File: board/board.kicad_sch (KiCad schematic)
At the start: 33 parts, among them J2 Conn_01x10, J3 Conn_01x06, J4 Conn_01x02, J5 Conn_01x06, J7 Conn_01x30, U2 nPM1300-QEAA, U3 MDBT50Q-P1MV2, Y1 32k Hz

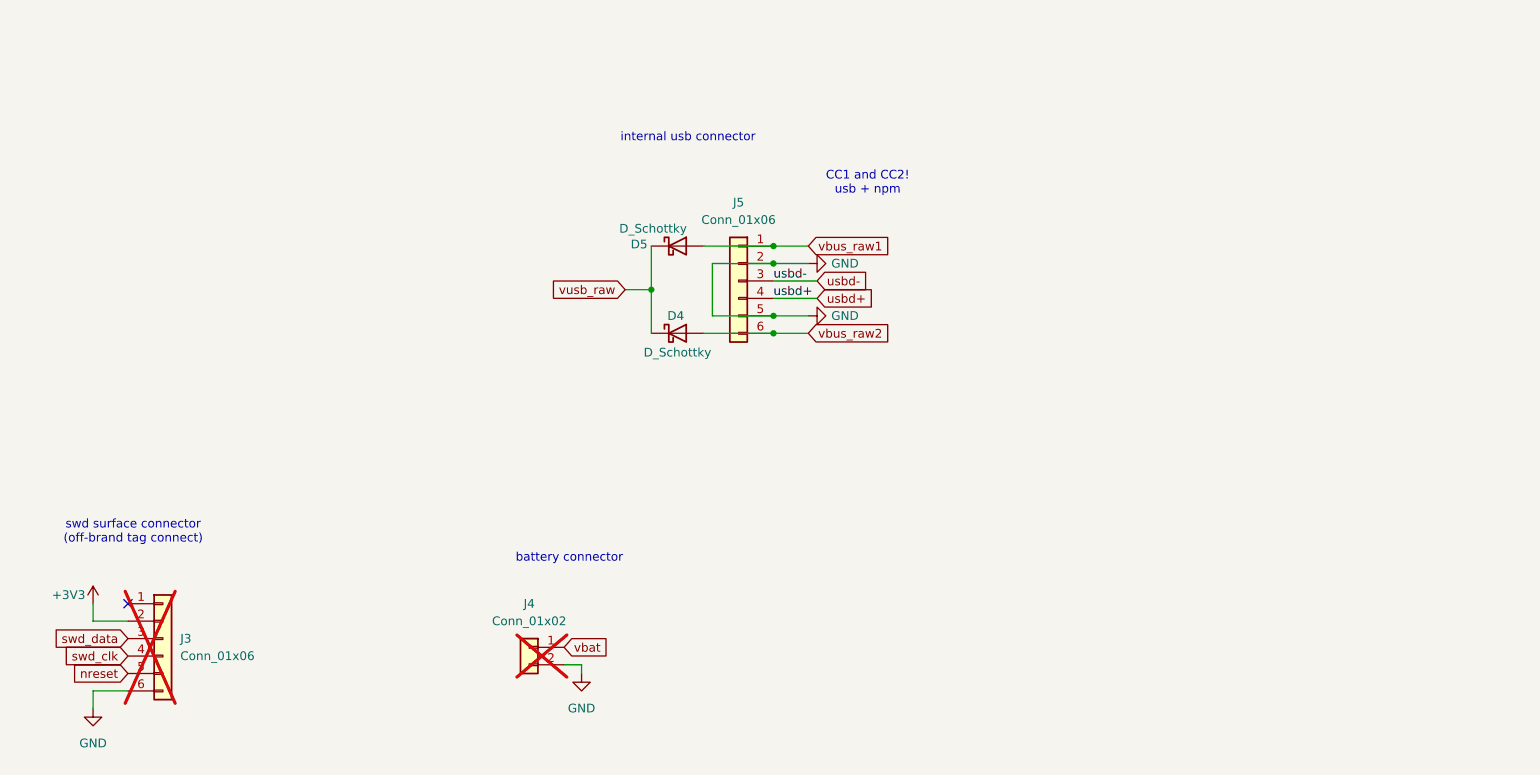
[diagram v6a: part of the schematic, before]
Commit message: board: sch add usb c to magnet adapter
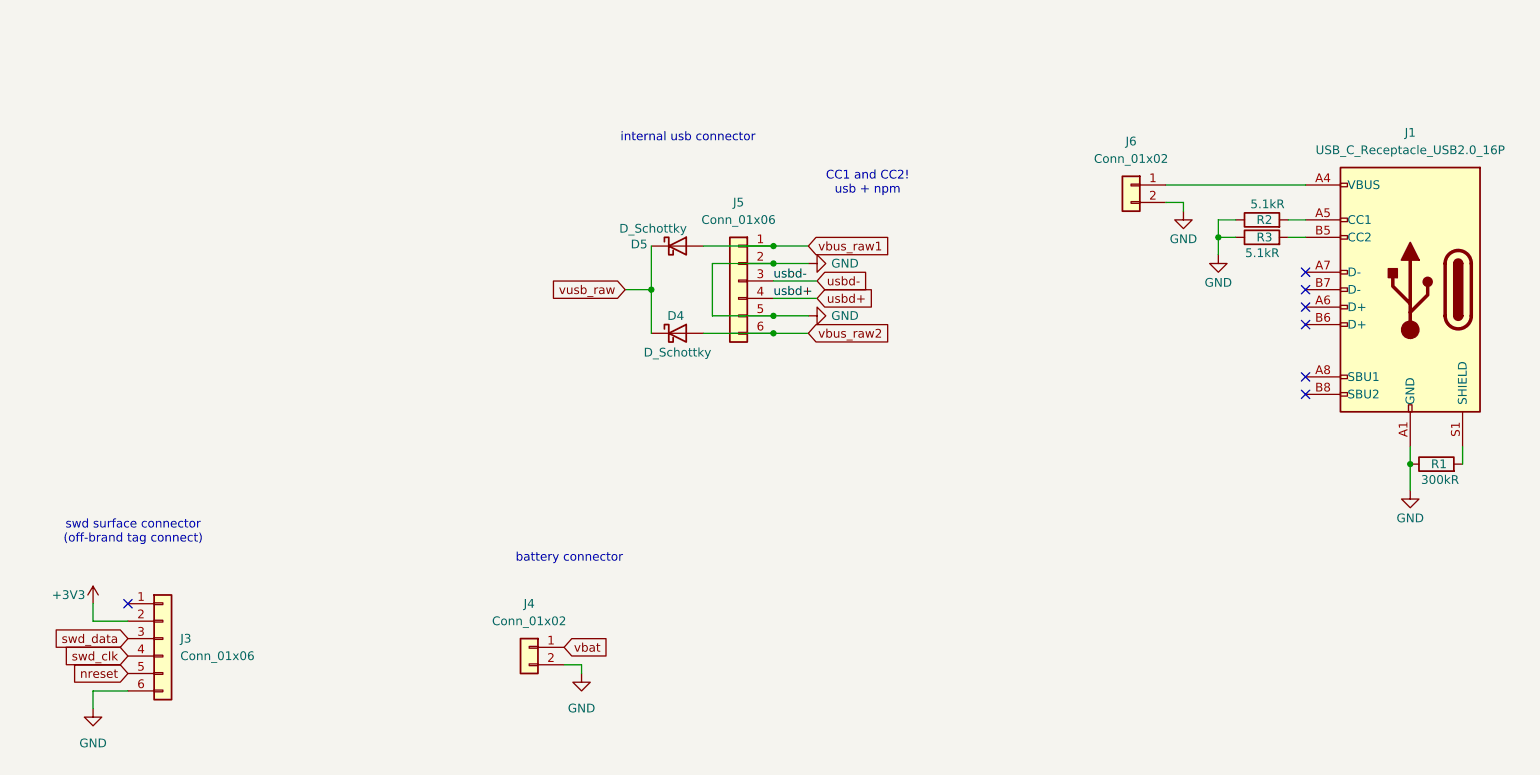
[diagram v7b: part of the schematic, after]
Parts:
- added J1: USB_C_Receptacle_USB2.0_16P, symbol Connector:USB_C_Receptacle_USB2.0_16P
- added J6: Conn_01x02, phiboard:magnetic connector 01x02P, symbol Connector_Generic:Conn_01x02
- added R1: 300kR, Resistor_SMD:R_0201_0603Metric, symbol Device:R
- added R2, R3: 5.1kR, Resistor_SMD:R_0201_0603Metric, symbol Device:R
- J3, J4: now fitted; now in the parts list
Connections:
- net GND: now also J1.A1 (GND), J1.A12 (GND), J1.B1 (GND), J1.B12 (GND), J6.2 (Pin_2), R1.1, R2.1, R3.1
- new net: J1.A4 (VBUS), J1.A9 (VBUS), J1.B4 (VBUS), J1.B9 (VBUS), J6.1 (Pin_1)
- new net: J1.S1 (SHIELD), R1.2
- new net: J1.B5 (CC2), R3.2
- new net: J1.A5 (CC1), R2.2
- no-connect marks 13 -> 19

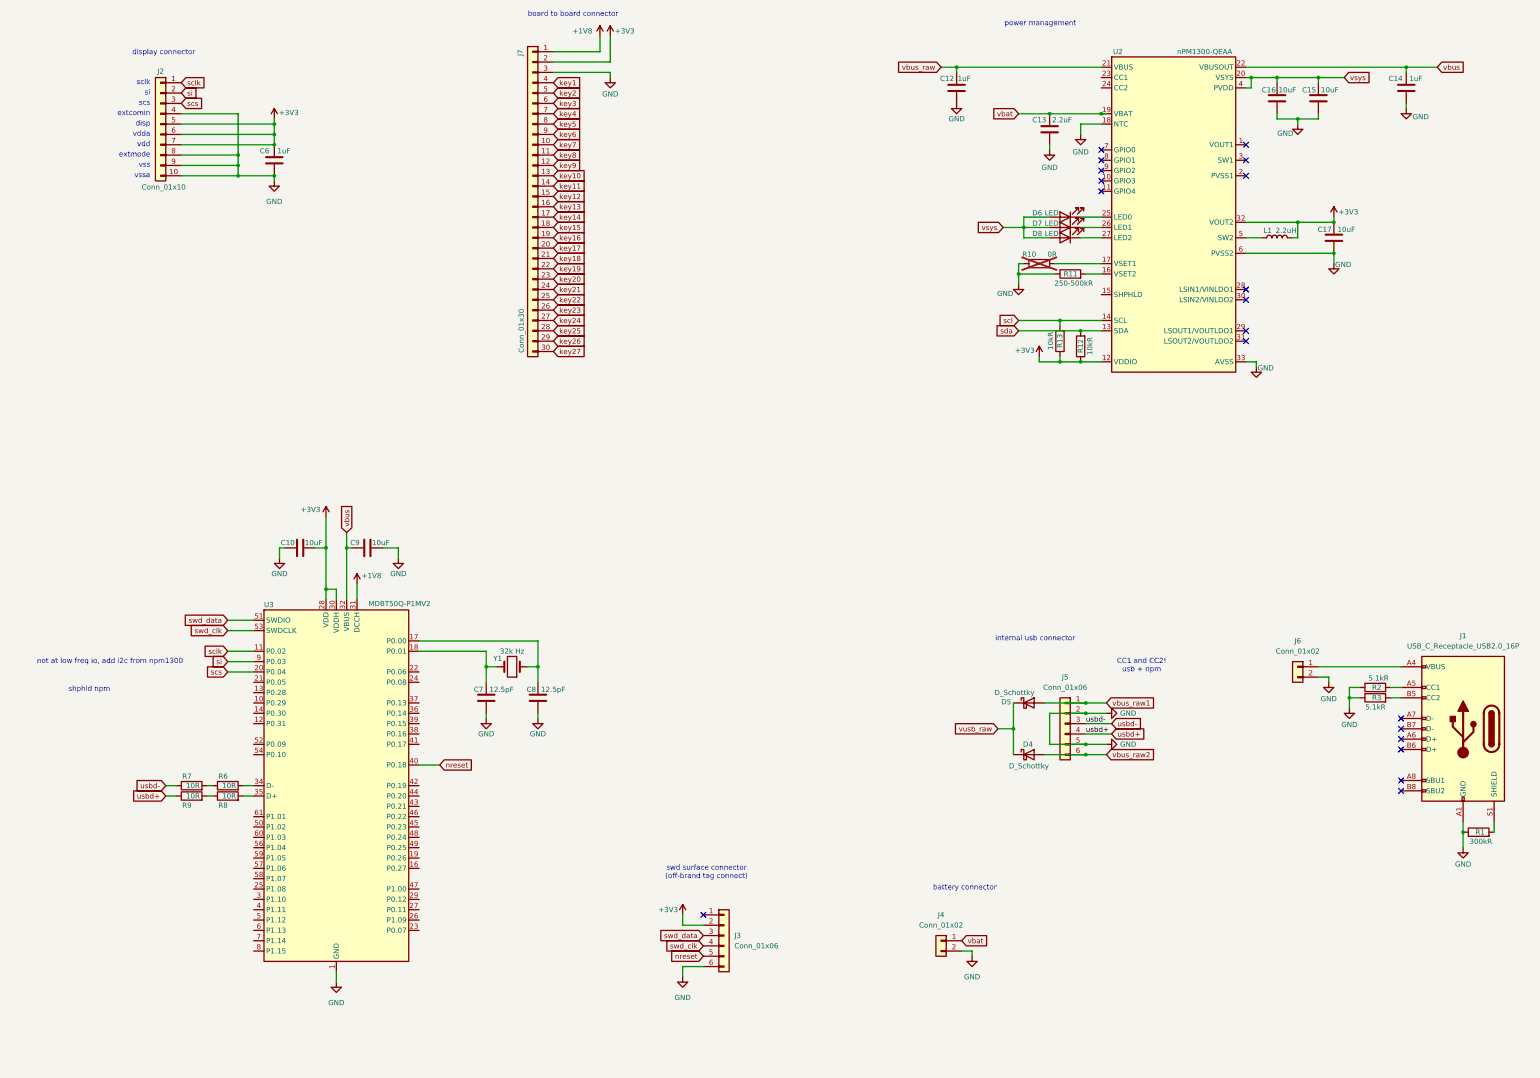
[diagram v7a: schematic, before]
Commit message: board: sch add usb circuit
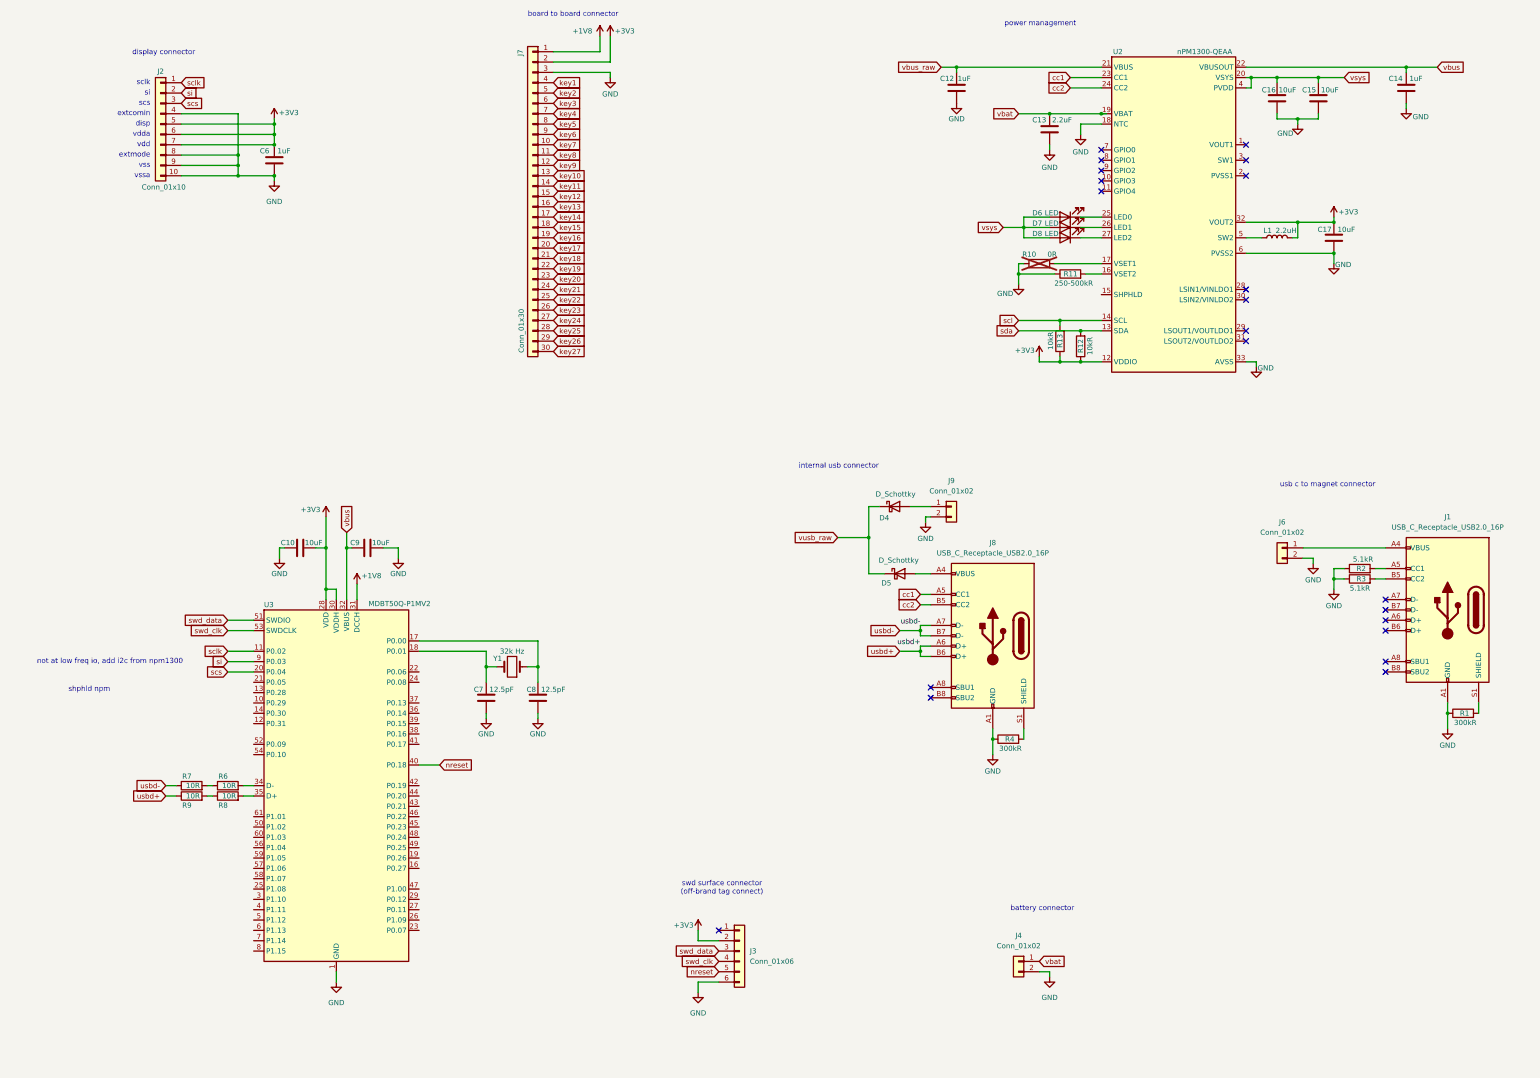
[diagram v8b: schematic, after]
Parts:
- removed J5: Conn_01x06, symbol Connector_Generic:Conn_01x06
- added J8: USB_C_Receptacle_USB2.0_16P, symbol Connector:USB_C_Receptacle_USB2.0_16P
- added J9: Conn_01x02, phiboard:magnetic connector 01x02P, symbol Connector_Generic:Conn_01x02
- added R4: 300kR, Resistor_SMD:R_0201_0603Metric, symbol Device:R
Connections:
- net GND: now also J8.A1 (GND), J8.A12 (GND), J8.B1 (GND), J8.B12 (GND), J9.2 (Pin_2), R4.1
- net usbd+: now also J8.A6 (D+), J8.B6 (D+)
- net usbd-: now also J8.A7 (D-), J8.B7 (D-)
- net cc1: now reaches U2.23 (CC1)
- net cc1: now also J8.A5 (CC1)
- net cc2: now reaches U2.24 (CC2)
- net cc2: now also J8.B5 (CC2)
- net vbus_raw1: no longer names the net of D5.2 (A)
- net vbus_raw1: now also J8.A4 (VBUS), J8.A9 (VBUS), J8.B4 (VBUS), J8.B9 (VBUS)
- net vbus_raw2: no longer names the net of D4.2 (A)
- net vbus_raw2: now also J9.1 (Pin_1)
- new net: J8.S1 (SHIELD), R4.2
- no-connect marks 19 -> 21
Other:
- note added: "usb c to magnet connector"
- note removed: "CC1 and CC2! usb + npm"
- moved on the sheet: D4, D5, J1, J3, J4, J6, R1, R2, R3
